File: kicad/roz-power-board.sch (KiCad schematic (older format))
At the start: 84 parts, among them CON1 USB-MICRO-B, J1 Jumper_Switch, J2 Jumper_Switch, J3 Jumper_Switch, J4 Jumper_Switch, J5 Jumper_Switch, J6 Jumper_Switch, J7 Jumper_Switch, J8 Jumper_Switch, P1 Wall, P10 GPIO_A5, P11 GPIO_A6, P12 GPIO_A7, P13 BIOLOID_BUS_1, P14 GPIO_B8, P15 GPIO_B9, P16 BIOLOID_BUS_2, P17 BIOLOID_BUS_3, P18 BIOLOID_BUS_4, P19 BIOLOID_BUS_5, P2 Battery, P20 BIOLOID_BUS_6, P21 rPi Power, P23 UART_BOOT, P25 BATT_BACKUP, P26 BUS, P3 BATT_BALANCE, P4 ALT_3.3_IN, P5 UART_1, P6 I2C_2, P7 SPI_2, P8 5V Regulator, P9 GPIO_A4, Q1 BS-170, Q2 STD30PF03LT4, Q3 STD30PF03LT4, SW1 Bus Power, SW2 PowerButton, SW3 RESET_SW, SW4 BOOT_SW, U1 LM3480-3.3, U2 LTC4412, U3 STM32F401xD_UFQFPN48, X1 32.768kHz, X2 8MHz

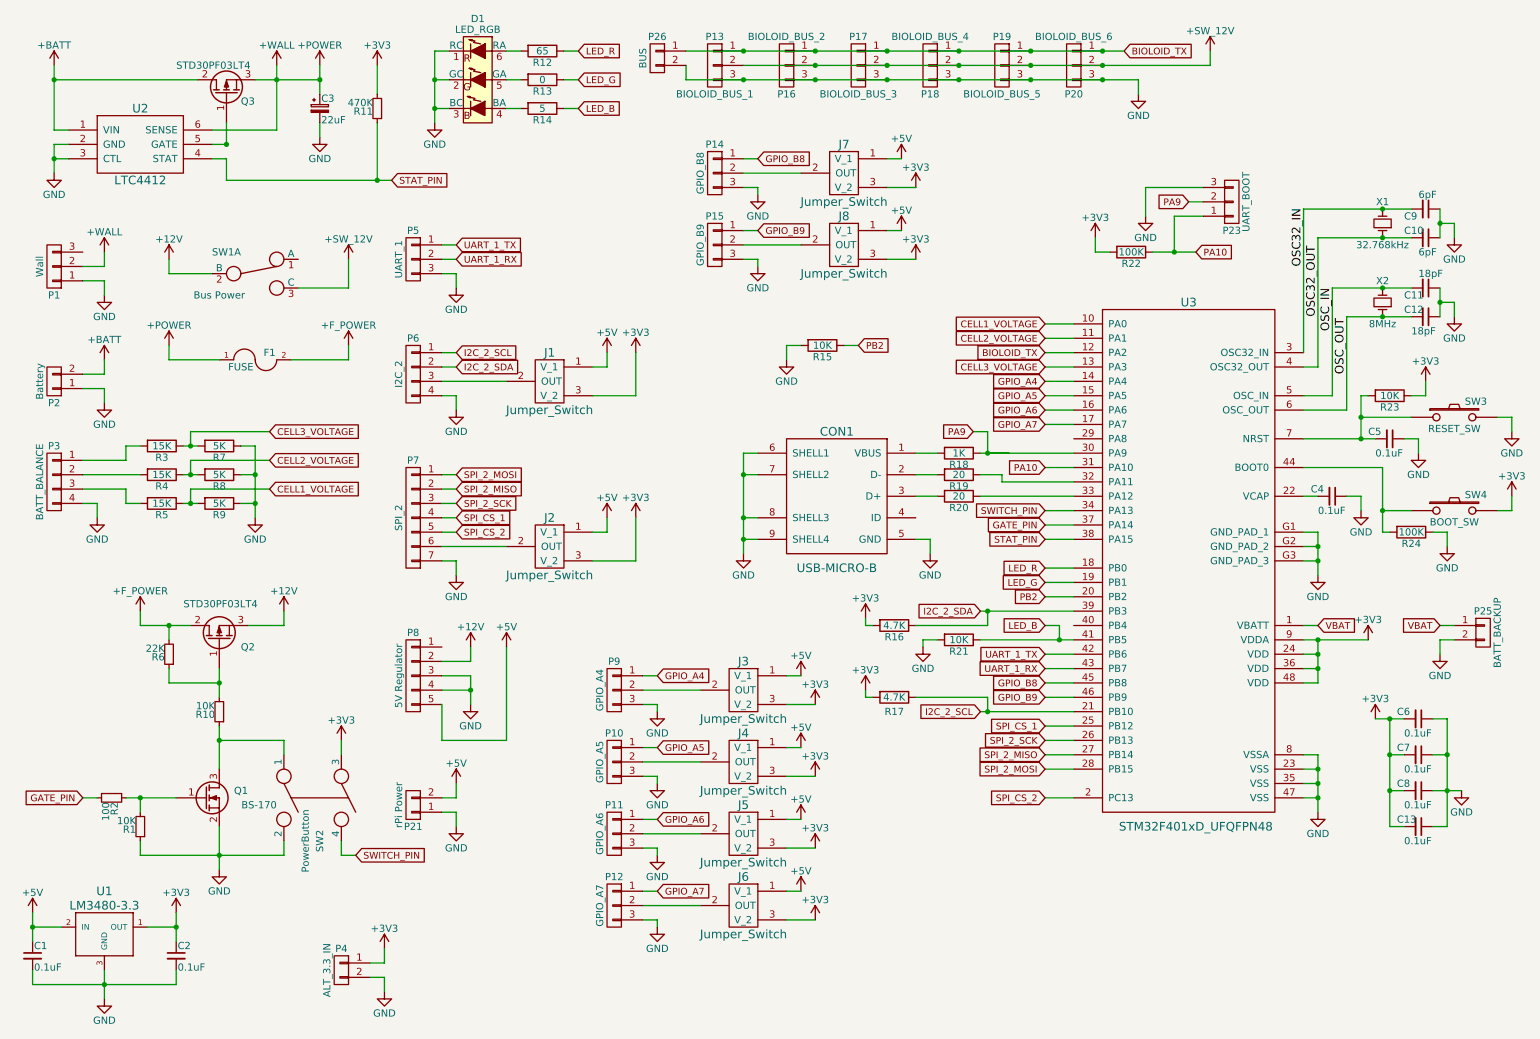
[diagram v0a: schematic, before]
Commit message: more fixes to power board pcb
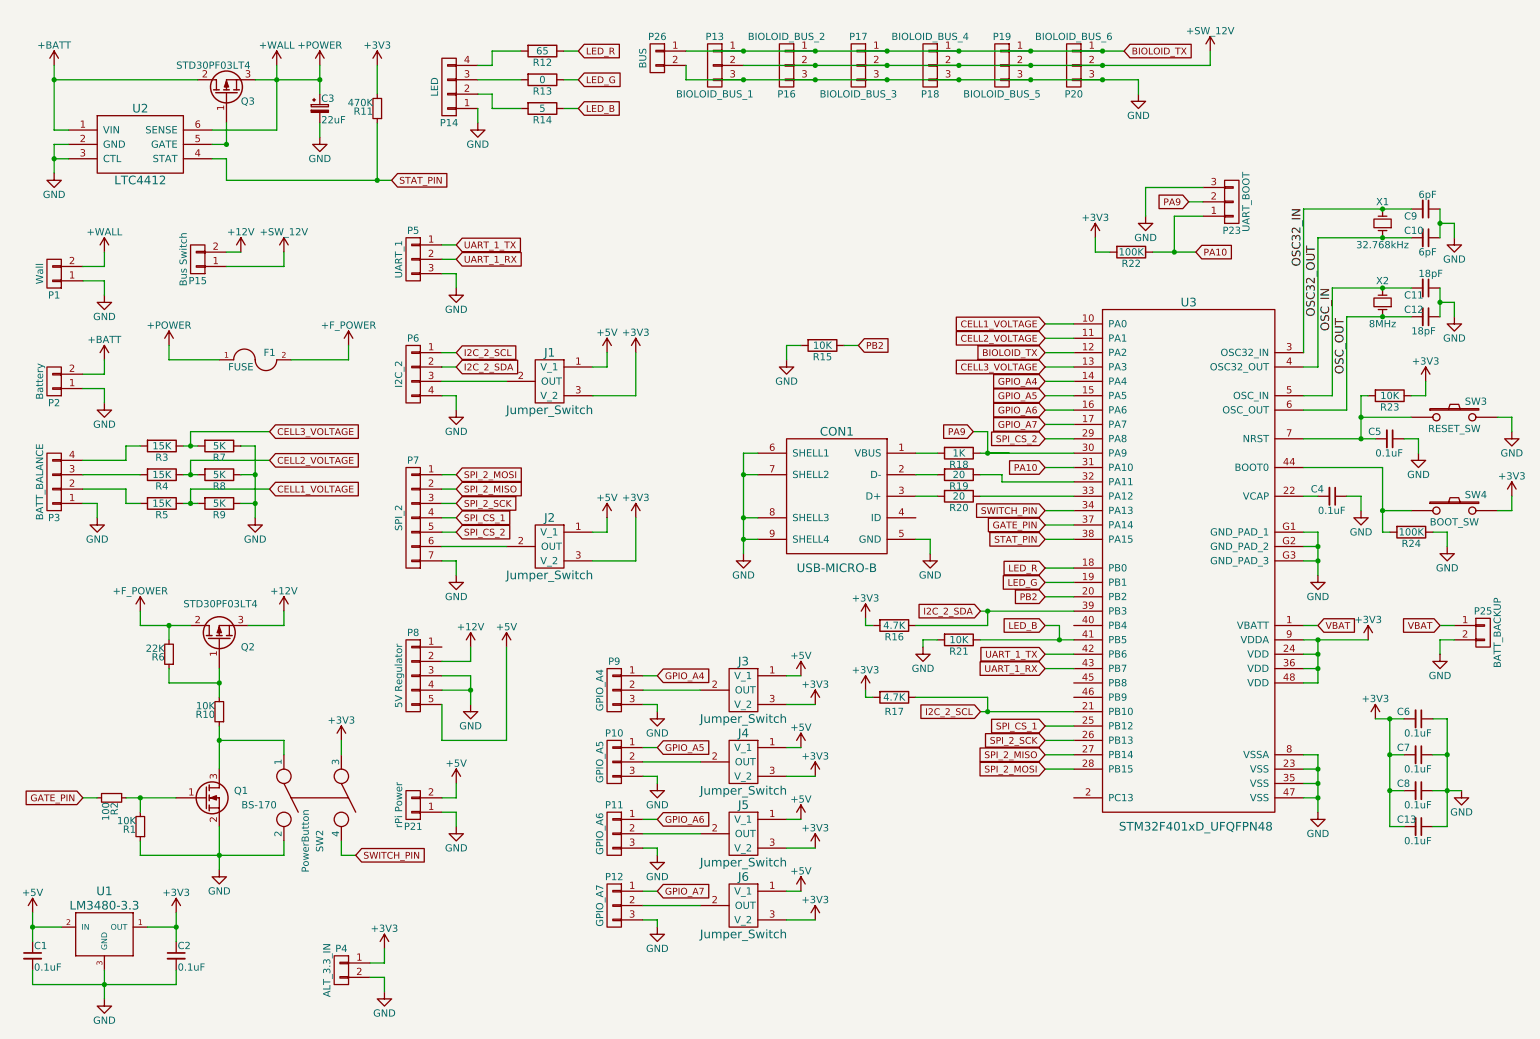
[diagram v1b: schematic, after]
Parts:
- removed D1: LED_RGB, LEDs:LED_RGB_PLLC-6, symbol LED_RGB
- removed J7, J8: Jumper_Switch, MicroPython-Parts-new:Jumper-Switch, symbol Jumper_Switch
- removed P1: Wall, MicroPython-Parts-new:PowerJack, symbol CONN_01X03
- removed P14: GPIO_B8, MicroPython-Parts-new:SIL_3_050, symbol CONN_01X03
- removed P15: GPIO_B9, MicroPython-Parts-new:SIL_3_050, symbol CONN_01X03
- removed SW1: Bus Power, MicroPython-Parts-new:RA-Switch-5Amp, symbol Switch_SPDT_x2
- added P1: Wall, MicroPython-Parts-new:TerminalBlock, symbol CONN_01X02
- added P14: LED, MicroPython-Parts-new:SIL_4_050, symbol CONN_01X04
- added P15: Bus Switch, MicroPython-Parts-new:TerminalBlock, symbol CONN_01X02
- SW2: footprint MicroPython-Parts-new:DPST_Mom_Switch -> MicroPython-Parts-new:SIL_4_050
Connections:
- net +12V: now also P15.2 (P2)
- net +POWER: now also P1.2 (P2)
- net +SW_12V: now also P15.1 (P1)
- net GND: now also P3.1 (P1), P1.1 (P1), P14.1 (P1); no longer P3.4 (P4)
- net SPI_CS_2: now also U3.29 (PA8); no longer U3.2 (PC13)
- net at R3.2: now also P3.4 (P4); no longer P3.1 (P1)
- net at P3.2 (P2): now also R5.2; no longer R4.2
- net at P3.3 (P3): now also R4.2; no longer R5.2
- net at R14.2: now also P14.2 (P2)
- net at R13.2: now also P14.3 (P3)
- net at R12.2: now also P14.4 (P4)
- net GPIO_B8: no longer names the net of U3.45 (PB8)
- net GPIO_B9: no longer names the net of U3.46 (PB9)

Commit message: more cleanup, changes
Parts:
- removed P23: UART_BOOT, MicroPython-Parts-new:SIL_3_050, symbol CONN_01X03
- added C14: 680uF, Capacitors_ThroughHole:C_Radial_D8_L21_P3.8, symbol CP_Small
- P1: value Wall -> Wall Power
- P21: value rPi Power -> rPi
- P25: value BATT_BACKUP -> VBAT
- P4: value ALT_3.3_IN -> ALT_3.3
- SW2: value PowerButton -> PowerSwitch
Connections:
- net +12V: now also C14.1
- net +5V: now also P21.1 (P1); no longer P21.2 (P2)
- net GND: now also P21.2 (P2), C14.2; no longer P21.1 (P1)

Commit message: rev 0.2 of the power board
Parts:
- removed U1: LM3480-3.3, TO_SOT_Packages_SMD:SOT-23, symbol LM3480IM3-5.0
- added P22: P_JUMP, Socket_Strips:Socket_Strip_Straight_1x02, symbol CONN_01X02
- added P23: USR_SW, MicroPython-Parts-new:SIL_2_050, symbol CONN_01X02
- added U1: AP7333, TO_SOT_Packages_SMD:SOT-23, symbol AP7333
- C3: footprint Capacitors_SMD:c_elec_3x5.3 -> Capacitors_SMD:c_elec_4x5.3
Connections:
- net +12V: now also Q2.2 (D); no longer Q2.3 (S)
- net +3V3: now also U1.2 (OUT)
- net +5V: now also U1.1 (IN)
- net +F_POWER: now also Q2.3 (S); no longer Q2.2 (D)
- net GND: now also P22.1 (P1), P23.1 (P1), U1.3 (GND)
- net at Q1.3 (D), R10.1, SW2.1: now also P22.2 (P2)
- net at U3.2 (PC13): now also P23.2 (P2)
- net BOOT0: now reaches R24.2, SW4.1, U3.44 (BOOT0)
- net BOOT0: now also U3.45 (PB8)
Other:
- moved on the sheet: P21, SW2
